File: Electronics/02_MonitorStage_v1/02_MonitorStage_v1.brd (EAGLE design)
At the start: 100 x 80 mm, 53 parts, among them J1 BARRIER_BLOCK-2PIN, J2 BARRIER_BLOCK-2PIN, J3 CONN_2X3_SMD, J4 CONN_2X3_SMD, J5 CONN_2X3_SMD, J6 CONN_2X3_SMD, J7 CONN_2X3_SMD, Q1 PN2222A-SOT-23

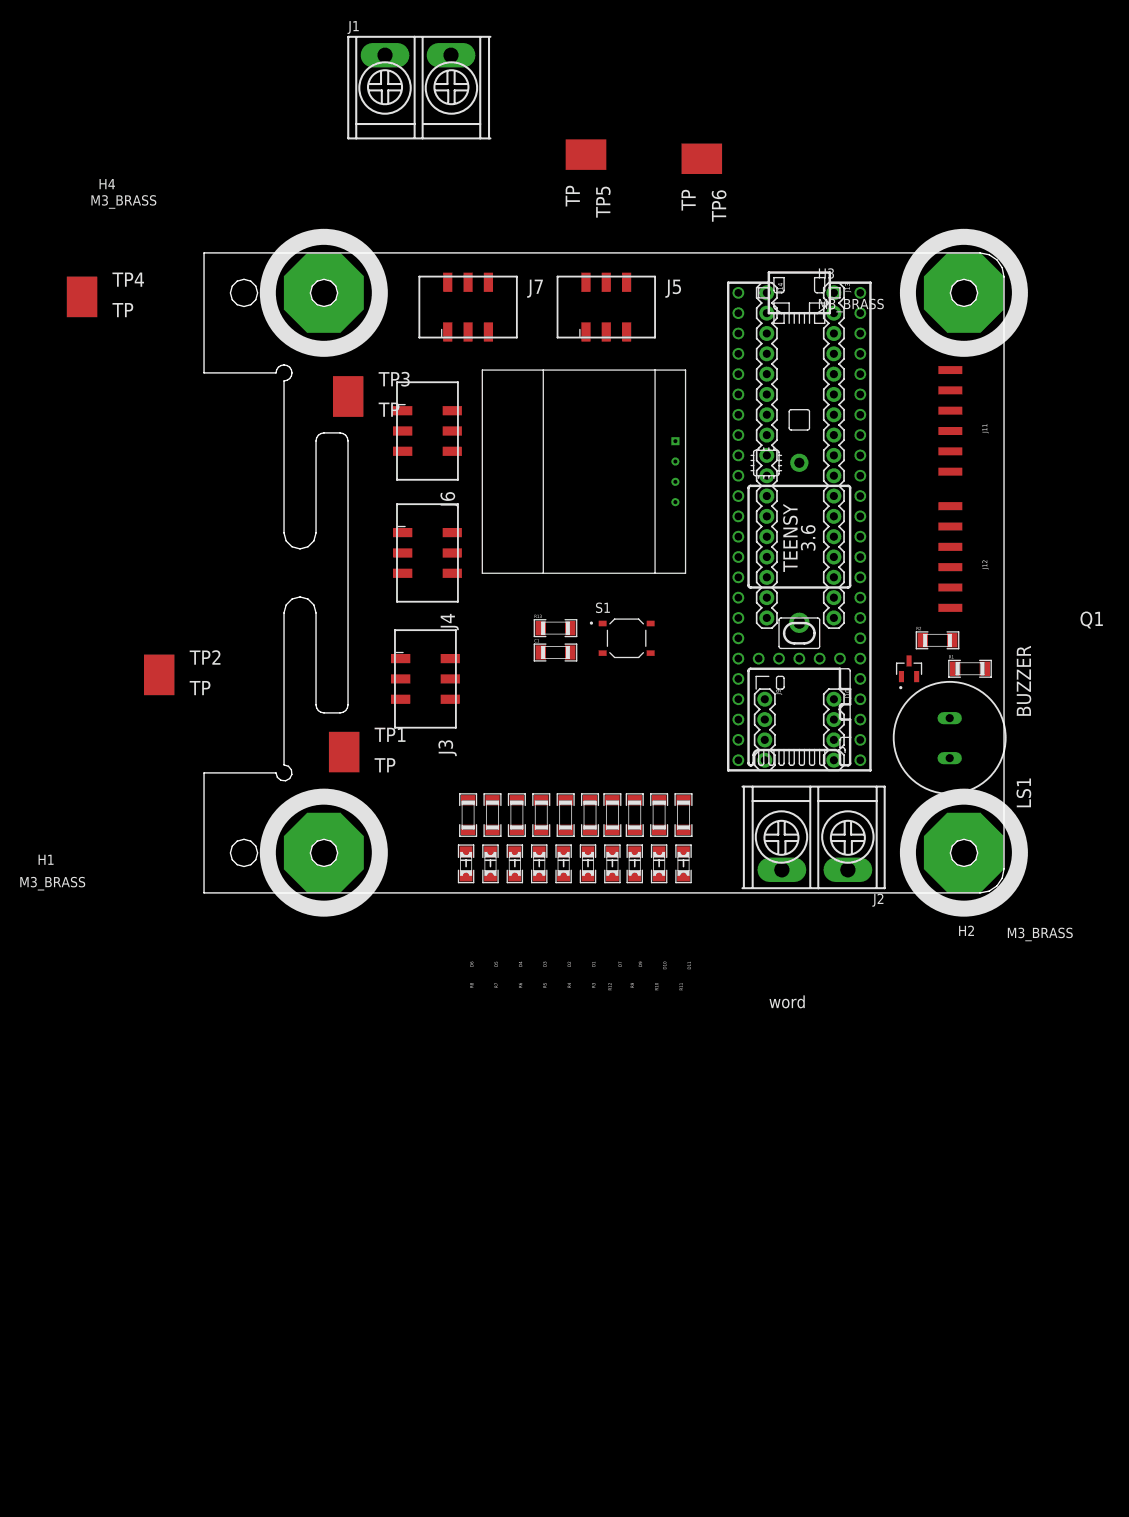
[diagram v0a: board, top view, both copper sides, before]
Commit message: Progress on monitor electronics schematic
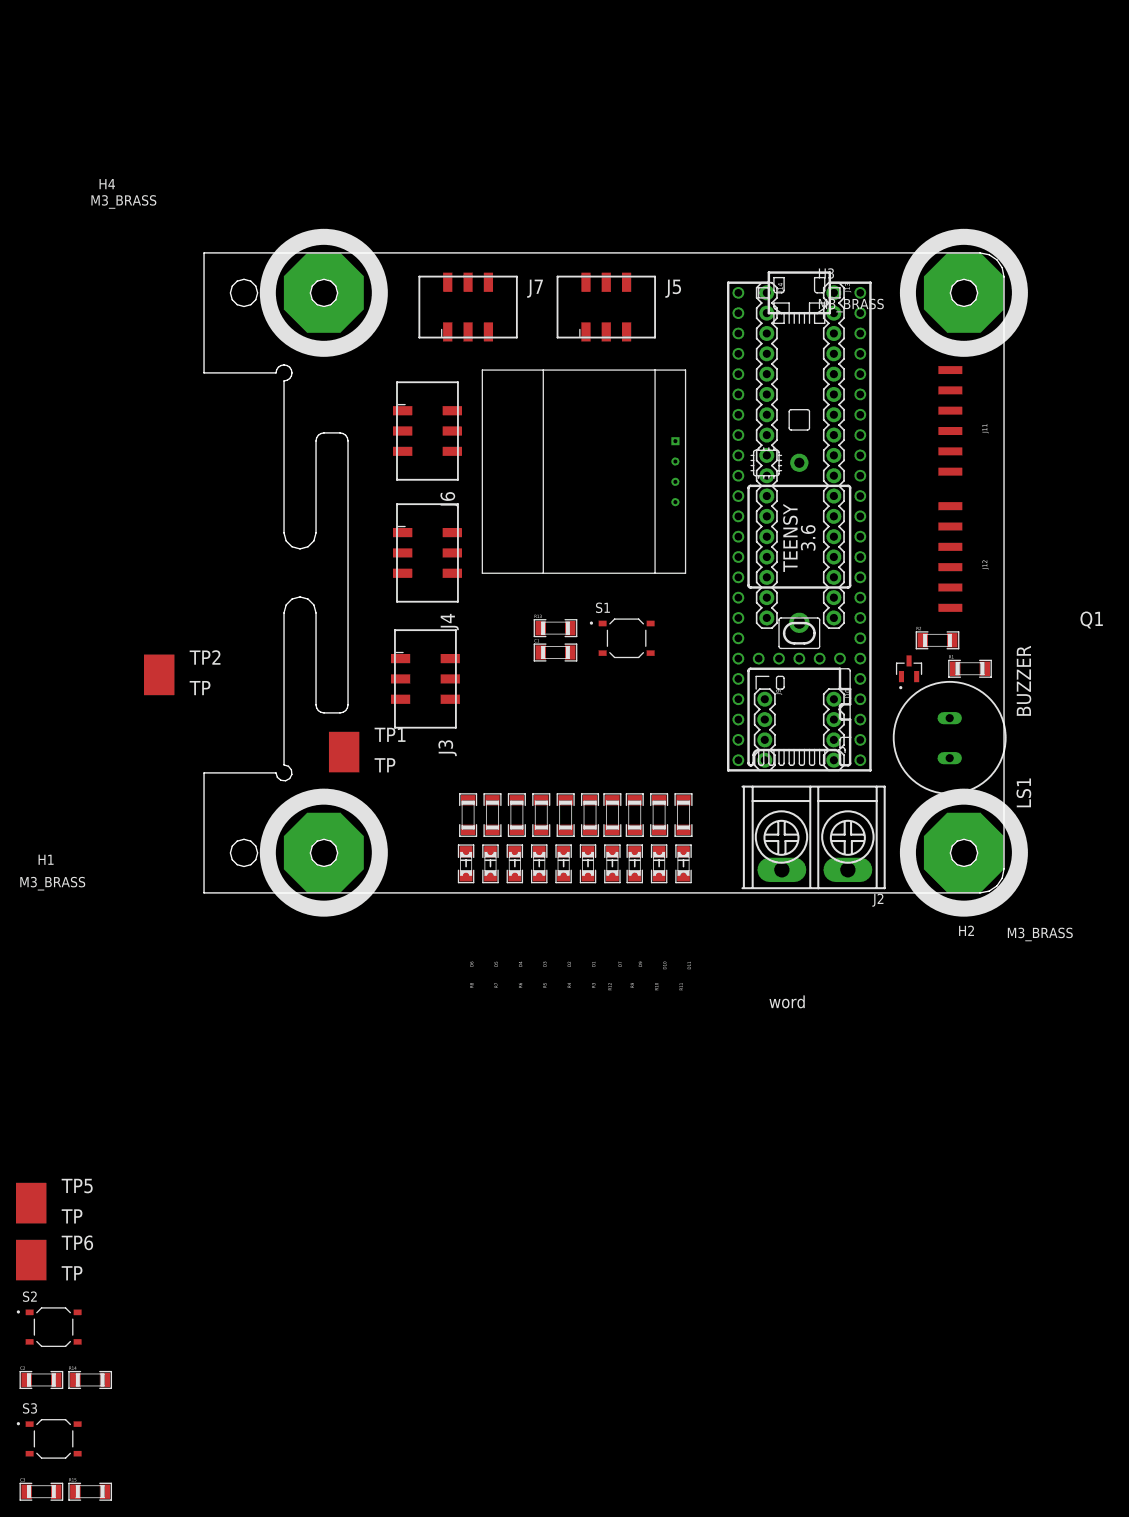
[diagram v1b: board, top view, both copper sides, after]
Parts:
- removed J1: BARRIER_BLOCK-2PIN, Hippo-PS:BARRIERBLOCK-2PIN
- removed TP3, TP4: TP, Hippo-PS:TP
- added C2, C3: 0.1uF, standardparts:1206
- added R14, R15: 1K, standardparts:1206
- added S2, S3: TACTILE_BUTTON, Hippo-PS:TACTILE_BUTTON
- C1: value (none) -> 0.1uF
- R13: value (none) -> 1K
- moved TP6 161.2 mm to (-4.32, -27.7), turned to 0 degrees
- moved TP5 148.3 mm to (-4.32, -20.6), turned to 0 degrees
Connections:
- new net +5V1: R1.2
- new net +5V_SIG: J6.3
- new net BUTTON2: C2.2, R14.2, S2.3, S2.4
- new net BUTTON3: C3.2, R15.2, S3.3, S3.4
- new net BUZZER: LS1.P$1, R2.1
- new net IN+_SIG: J6.1
- new net N$1: BT1.+, U$1.VBAT
- new net N$10: D9.P$1, R9.2
- new net N$11: D10.P$1, R10.2
- new net N$12: D11.P$1, R11.2
- new net N$13: LS1.P$2, Q1.COLLECTOR, R1.1
- new net N$14: R3.1
- new net N$15: R4.1
- new net N$16: R5.1
- new net N$17: R6.1
- new net N$18: R7.1
- new net N$19: R8.1
- new net N$2: D1.P$1, R3.2
- new net N$20: R9.1
- new net N$21: R10.1
- new net N$22: R11.1
- new net N$23: Q1.BASE, R2.2
- new net N$3: D2.P$1, R4.2
- new net N$5: D3.P$1, R5.2
- new net N$7: D4.P$1, R6.2
- new net N$8: D5.P$1, R7.2
- new net N$9: D6.P$1, R8.2
- new net S03_SIG1: J7.2
- new net S03_SIG2: J7.1
- new net S03_SIG3: J7.3
- new net S03_SIG4: J7.5
- new net S03_SIGSMPS: J7.4
- new net S04_SIG1: J3.4
- new net S04_SIG2: J3.5
- new net S04_SIG3: J3.3
- new net S04_SIGSMPS: J3.1
- new net S05_SIG1: J4.3
- new net S05_SIG2: J4.5
- new net S05_SIGNP: J4.4
- new net S05_SIGSMPS: J4.1
- new net S06_SIG1: J5.5
- new net S06_SIGSMPS: J5.4
- net +5V: now also J2.P$1, J6.4, U$1.VIN
- net GND: now also BT1.-, C2.1, C3.1, D1.P$2, D10.P$2, D11.P$2, D2.P$2, D3.P$2, D4.P$2, D5.P$2, D6.P$2, D9.P$2, J3.6, J4.6, J5.6, J6.6, J7.6, Q1.EMITTER, R14.1, R15.1, U$2.GND; no longer J1.P$2, TP4.P$1
- net IN+: no longer J2.P$1
- net N$4: now also S2.1, S2.2, S3.1, S3.2
- net V+: now also U$1.3V3, U$2.VCC; no longer J1.P$1, TP3.P$1

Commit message: Routed monitor stage board
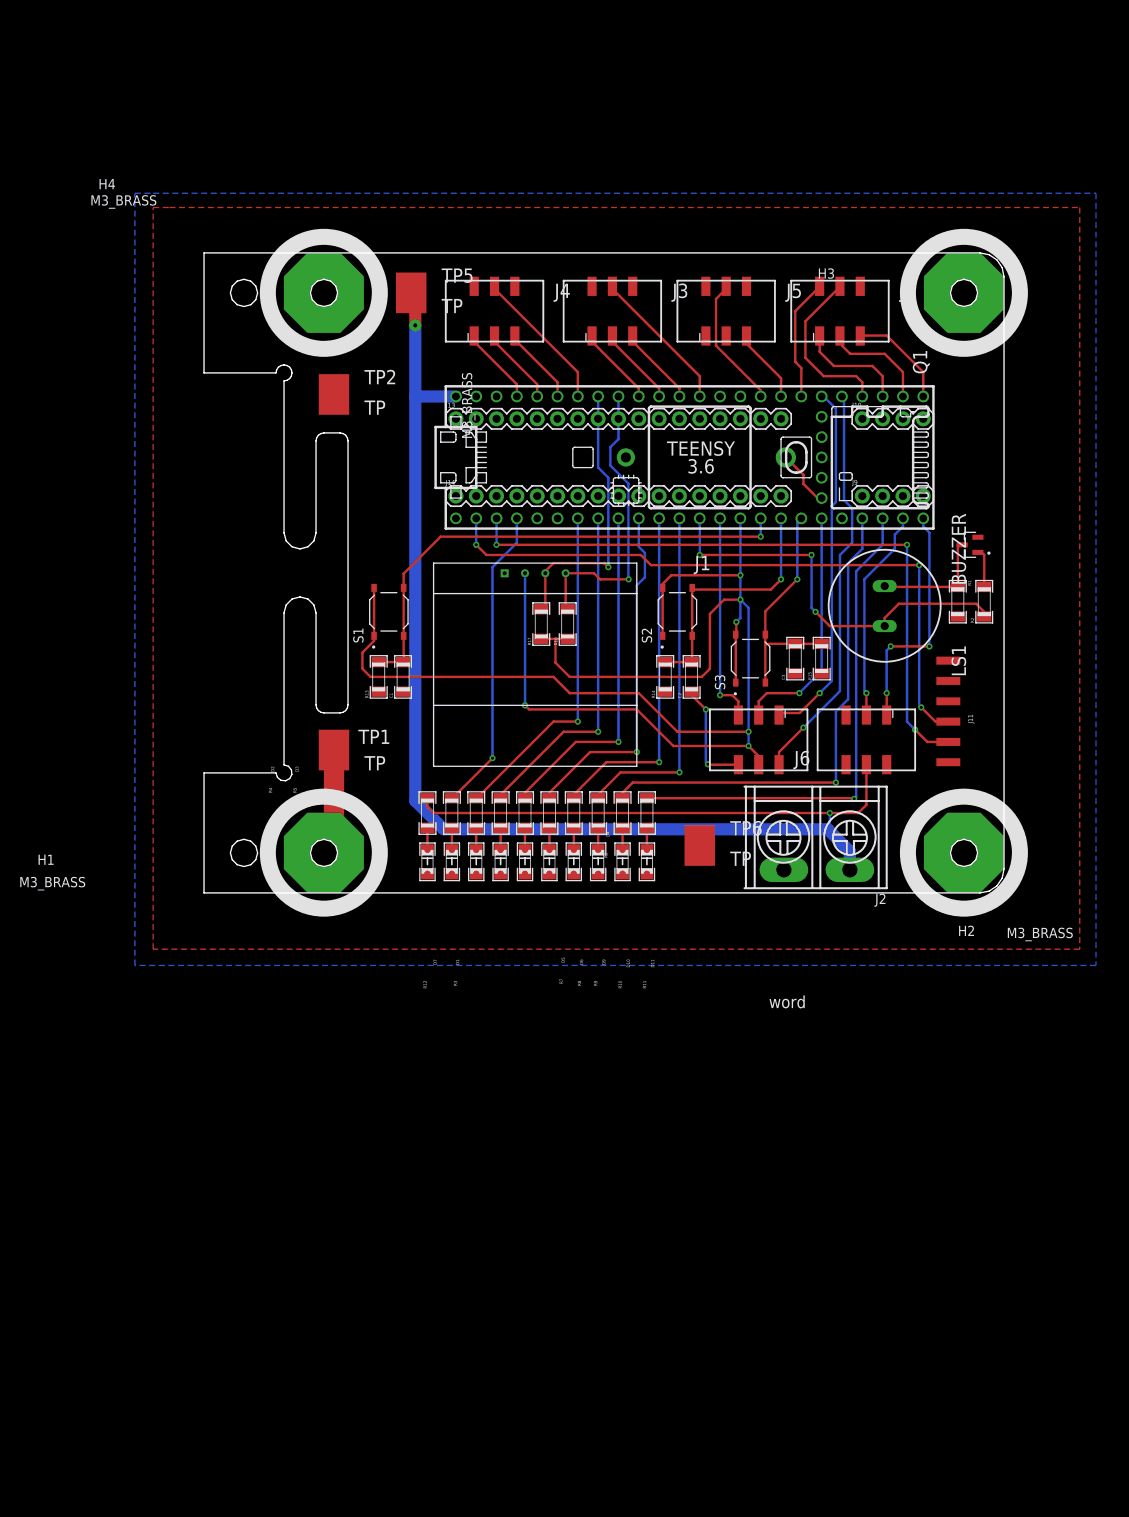
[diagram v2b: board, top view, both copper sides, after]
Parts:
- removed J12: (no value), Hippo-PS:1X06-SMD_RA_MALE_NO_HOLES
- added J1: CONN_2X3_SMD, Hippo-PS:2X3_SMD_CONNECTOR
- added R16, R17: 4.7K, standardparts:1206
- moved C3 140.4 mm to (91.2, 47.5), turned to 90 degrees
- moved R15 138.6 mm to (94.5, 47.5), turned to 90 degrees
- moved S3 130.8 mm to (85.6, 47.5), turned to 90 degrees
- moved TP5 123.3 mm to (43.2, 93.2)
- moved C2 119.7 mm to (78.2, 45.2), turned to 90 degrees
- moved S2 118.6 mm to (76.5, 53.3), turned to 90 degrees
- moved R14 113.5 mm to (74.9, 45.2), turned to 90 degrees
- moved TP6 98.3 mm to (79.2, 24.1)
- moved J6 67.1 mm to (100.1, 37.3), turned to 180 degrees
- moved J3 51.6 mm to (68.3, 90.9), turned to 0 degrees
- moved U$2 49.9 mm to (46.0, 34.0), turned to 0 degrees
- moved J13 49.8 mm to (48.8, 77.5), turned to 0 degrees
- moved J7 46.5 mm to (96.8, 90.9)
- moved J14 46.4 mm to (48.8, 67.8), turned to 0 degrees
- moved TP2 41.3 mm to (33.5, 80.5)
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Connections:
- removed net N$14: R3.1
- removed net N$15: R4.1
- removed net N$16: R5.1
- removed net N$17: R6.1
- removed net N$18: R7.1
- removed net N$19: R8.1
- removed net N$20: R9.1
- removed net N$21: R10.1
- removed net N$22: R11.1
- removed net N$4: S1.1, S1.2, S2.1, S2.2, S3.1, S3.2
- new net FREE1: J1.5, U$1.12/MISO
- new net FREE2: J1.3, U$1.27
- new net FREE3: U$1.28
- new net LED: U$1.13/SCK
- new net LED_S01: R4.1, U$1.5
- new net LED_S03: R5.1, U$1.6
- new net LED_S03A: R10.1, U$1.29
- new net LED_S03B: R11.1, U$1.30
- new net LED_S03C: R3.1, U$1.2
- new net LED_S03D: R9.1, U$1.10/CS
- new net LED_S04: R6.1, U$1.7
- new net LED_S05: R7.1, U$1.8
- new net LED_S06: R8.1, U$1.9/CS
- new net RX1: J11.3, U$1.0/RX
- new net SCL: J13.8, R17.2, U$1.19/A5/SCL, U$2.SCL
- new net SCL1: J1.2, U$1.37/A18
- new net SCL2: U$1.3/CANTX
- new net SDA: J13.9, R16.2, U$1.18/A4/SDA, U$2.SDA
- new net SDA1: J1.1, U$1.38/A19
- new net SDA2: U$1.4/CANRX
- new net TX1: J11.2, U$1.1/TX
- net +5V_SIG: now also U$1.31/A12
- net BUTTON1: now also U$1.24
- net BUTTON2: now also U$1.25
- net BUTTON3: now also U$1.26
- net BUZZER: now also U$1.11/MOSI
- net GND: now also J1.6, J11.6, U$1.GND, U$1.GND2
- net IN+_SIG: now also U$1.32/A13
- net S03_SIG1: now also U$1.39/A20
- net S03_SIG2: now also U$1.35/A16
- net S03_SIG3: now also U$1.34/A15
- net S03_SIG4: now also U$1.33/A14
- net S03_SIGSMPS: now also U$1.36/A17
- net S04_SIG1: now also U$1.14/A0
- net S04_SIG2: now also U$1.15/A1
- net S04_SIG3: now also U$1.16/A2
- net S04_SIGSMPS: now also U$1.17/A3
- net S05_SIG1: now also U$1.22/A8
- net S05_SIG2: now also U$1.21/A7
- net S05_SIGNP: now also U$1.20/A6
- net S05_SIGSMPS: now also U$1.23/A9
- net S06_SIG1: now also U$1.21/DAC0
- net S06_SIGSMPS: now also U$1.A22/DAC1
- net V+: now also J1.4, R16.1, R17.1, S1.1, S1.2, S2.1, S2.2, S3.1, S3.2
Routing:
- net V+: track 0.00 -> 205.9 mm, vias 0 -> 6
- net +5V: track 0.00 -> 191.9 mm, vias 0 -> 2
- net TX1: track 0.00 -> 82.9 mm, vias 0 -> 3
- net RX1: track 0.00 -> 81.7 mm, vias 0 -> 3
- net BUTTON1: track 0.00 -> 63.0 mm, vias 0 -> 1
- net LED_S03B: track 0.00 -> 62.5 mm, vias 0 -> 1
- net LED_S03A: track 0.00 -> 62.3 mm, vias 0 -> 1
- net BUZZER: track 0.00 -> 50.4 mm, vias 0 -> 3
- net SCL1: track 0.00 -> 50.3 mm, vias 0 -> 1
- net SDA1: track 0.00 -> 45.0 mm, vias 0 -> 1
- net LED_S05: track 0.00 -> 43.7 mm, vias 0 -> 1
- net LED_S03D: track 0.00 -> 43.5 mm, vias 0 -> 1
- net LED_S06: track 0.00 -> 43.3 mm, vias 0 -> 1
- net LED_S04: track 0.00 -> 42.9 mm, vias 0 -> 1
- net LED_S03: track 0.00 -> 42.6 mm, vias 0 -> 1
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- added copper zone on layer 1, net GND
- added copper zone on layer 16, net GND

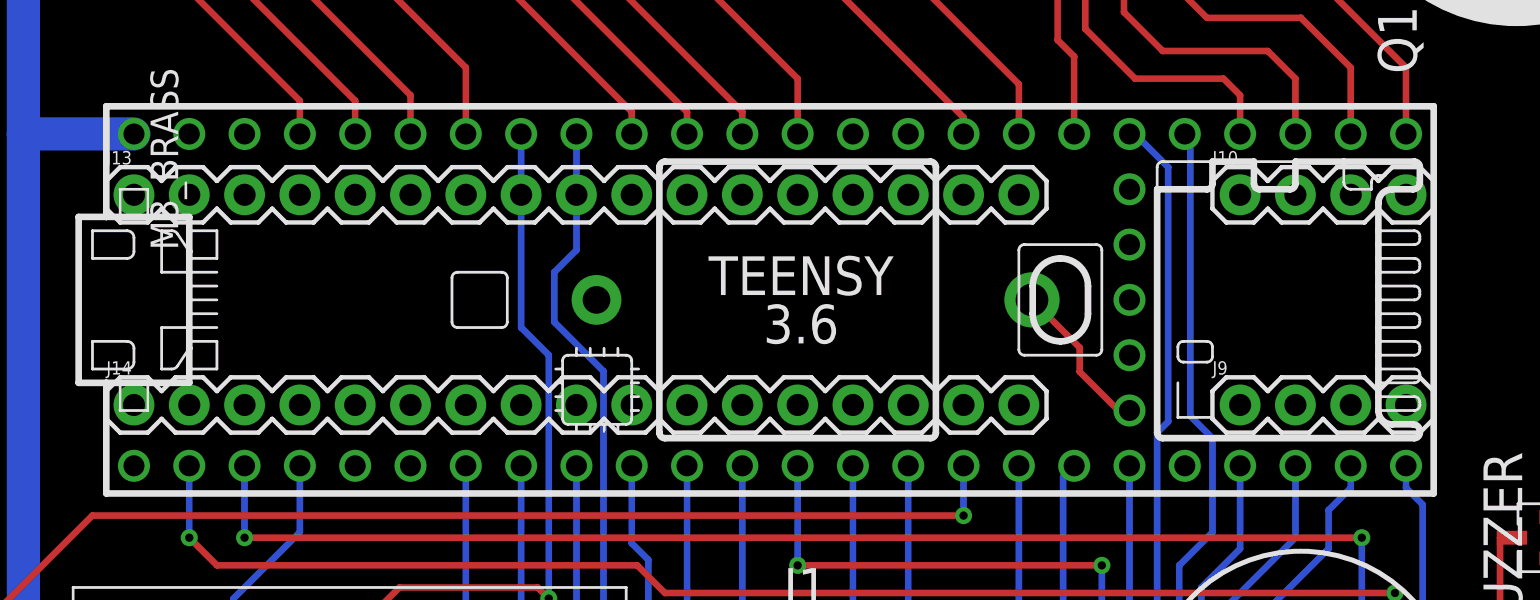
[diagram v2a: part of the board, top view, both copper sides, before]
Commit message: Routing improvements on monitor stage electronics
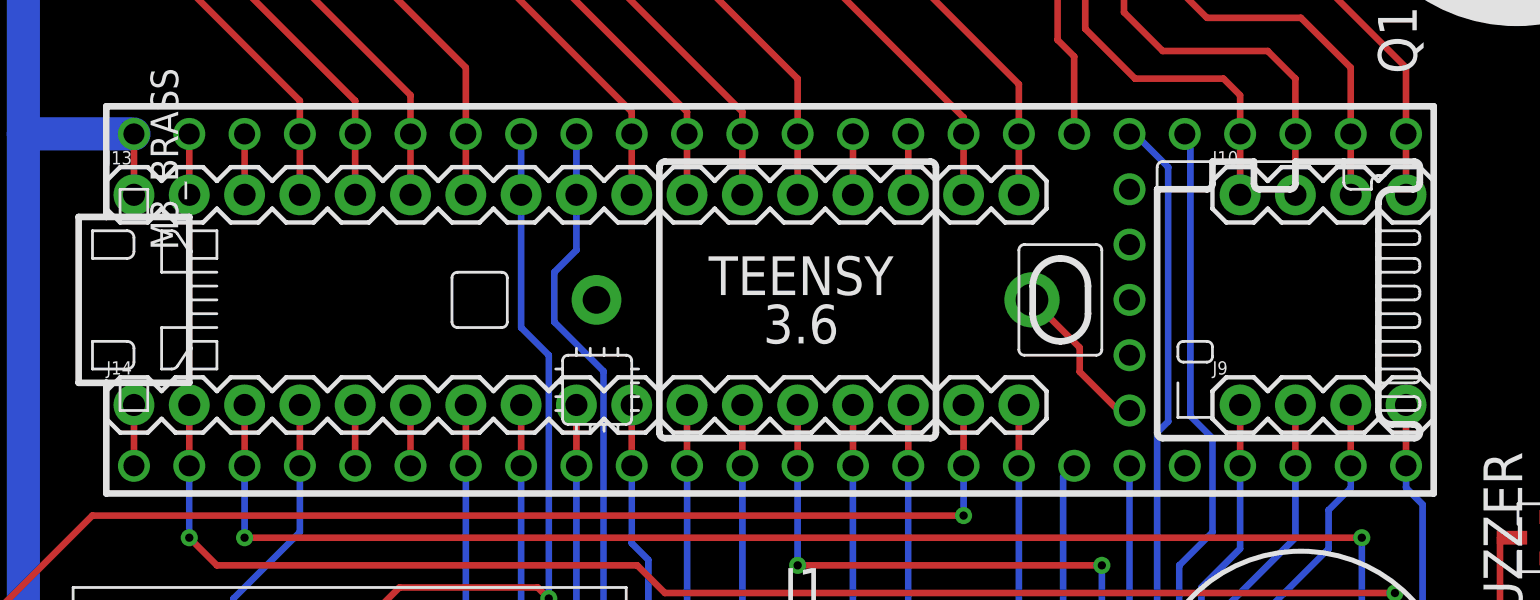
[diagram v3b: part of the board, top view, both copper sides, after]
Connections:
- new net N$14: J13.3, U$1.3V3_LO
- new net N$4: J13.2, U$1.AGND
- net +5V: now also J13.1
- net +5V_SIG: now also J9.3
- net BUTTON1: now also J14.16
- net BUTTON2: now also J14.17
- net BUZZER: now also J14.13
- net FREE1: now also J14.14
- net GND: now also J13.15, J14.1
- net IN+_SIG: now also J9.4
- net LED: now also J13.14
- net LED_S01: now also J14.7
- net LED_S03: now also J14.8
- net LED_S03A: now also J9.1
- net LED_S03B: now also J9.2
- net LED_S03C: now also J14.4
- net LED_S03D: now also J14.12
- net LED_S04: now also J14.9
- net LED_S05: now also J14.10
- net LED_S06: now also J14.11
- net RX1: now also J14.2
- net S03_SIG2: now also J10.2
- net S03_SIG3: now also J10.3
- net S03_SIG4: now also J10.4
- net S03_SIGSMPS: now also J10.1
- net S04_SIG1: now also J13.13
- net S04_SIG2: now also J13.12
- net S04_SIG3: now also J13.11
- net S04_SIGSMPS: now also J13.10
- net S05_SIG1: now also J13.5
- net S05_SIG2: now also J13.6
- net S05_SIGNP: now also J13.7
- net S05_SIGSMPS: now also J13.4
- net S06_SIG1: now also J13.17
- net S06_SIGSMPS: now also J13.16
- net SCL2: now also J14.5
- net SDA2: now also J14.6
- net TX1: now also J14.3
- net V+: now also J14.15
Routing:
- net GND: track 13.7 -> 19.3 mm
- net IN+_SIG: track 29.9 -> 32.7 mm
- net S03_SIG2: track 13.7 -> 16.4 mm
- net TX1: track 82.9 -> 85.7 mm
- net SDA2: track 0.00 -> 2.79 mm
- net SCL2: track 0.00 -> 2.79 mm
- net S06_SIGSMPS: track 16.6 -> 19.4 mm
- net S06_SIG1: track 9.35 -> 12.1 mm
- net S05_SIGSMPS: track 9.77 -> 12.6 mm
- net S05_SIGNP: track 18.1 -> 20.9 mm
- net S05_SIG2: track 9.77 -> 12.6 mm
- net S05_SIG1: track 9.77 -> 12.6 mm
- net S04_SIGSMPS: track 9.98 -> 12.8 mm
- net S04_SIG3: track 9.98 -> 12.8 mm
- net S04_SIG2: track 9.98 -> 12.8 mm
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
